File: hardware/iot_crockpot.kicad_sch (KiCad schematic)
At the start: 0 parts

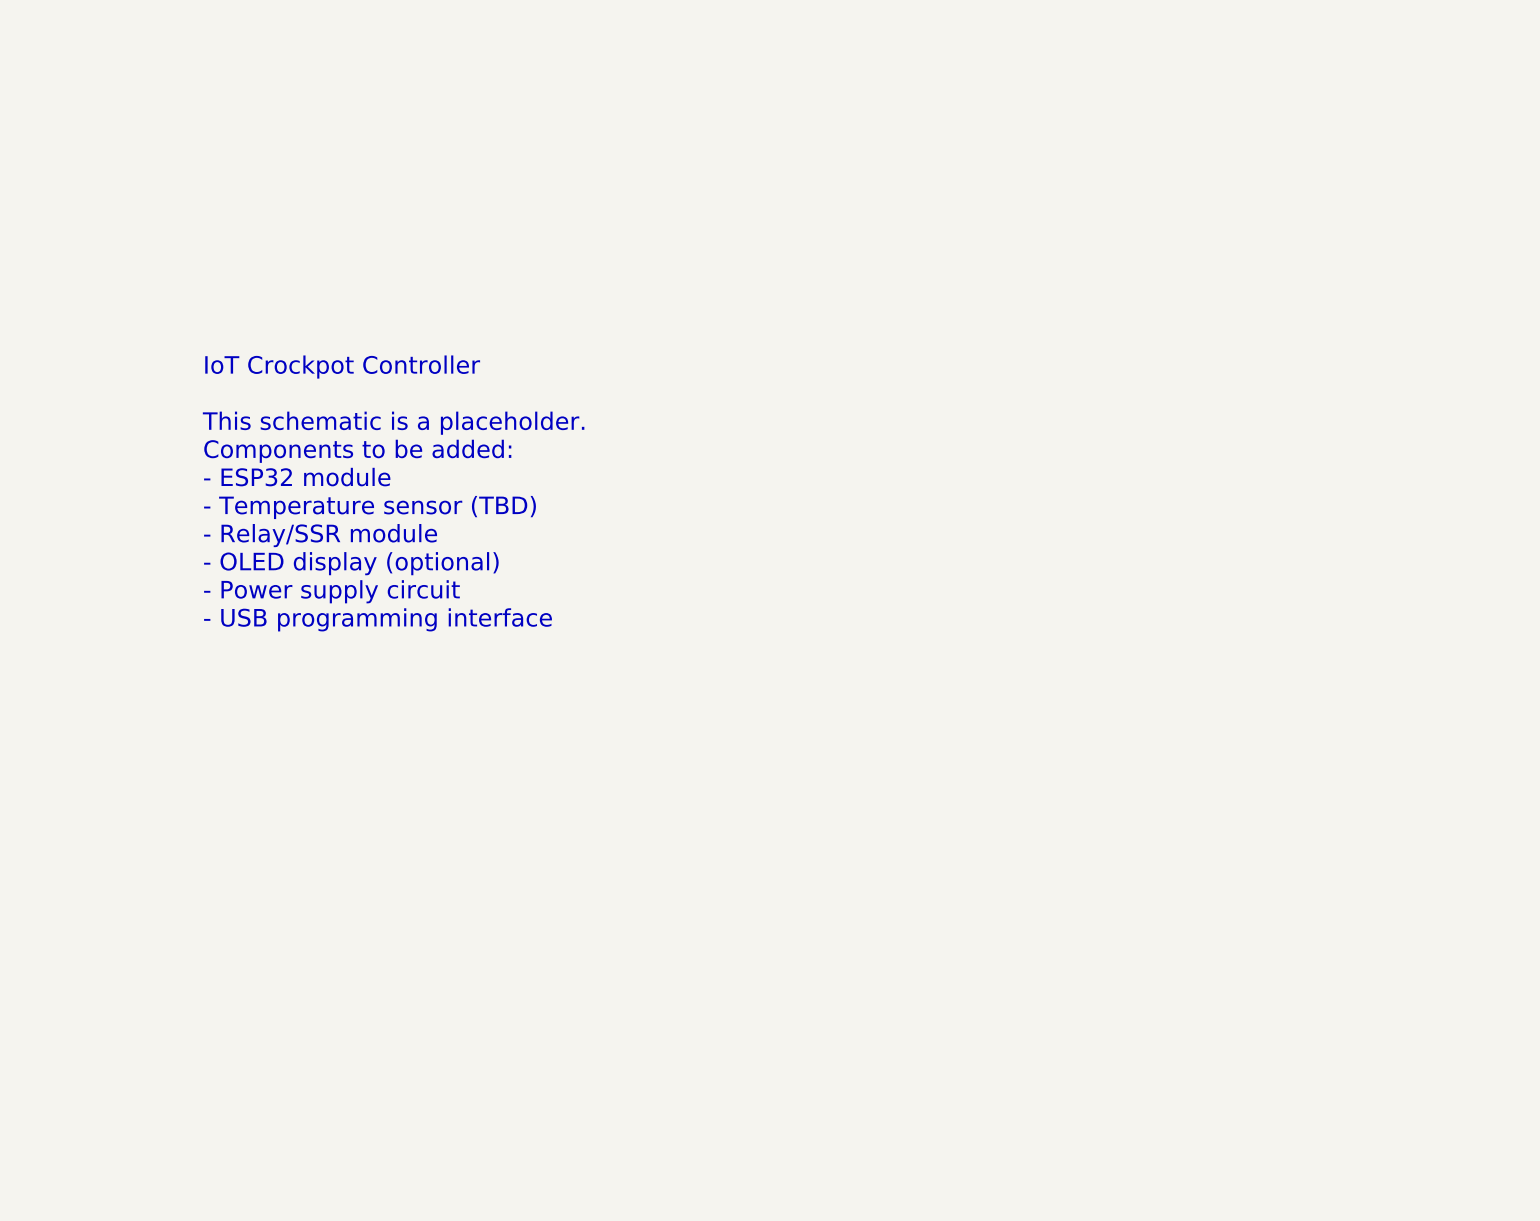
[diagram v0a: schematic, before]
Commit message: Started schematic part selection
added XIAO ESP32-C3
added HLK-PM01 120VAC to 5VDC power module
added relays
added thermal couple sensor
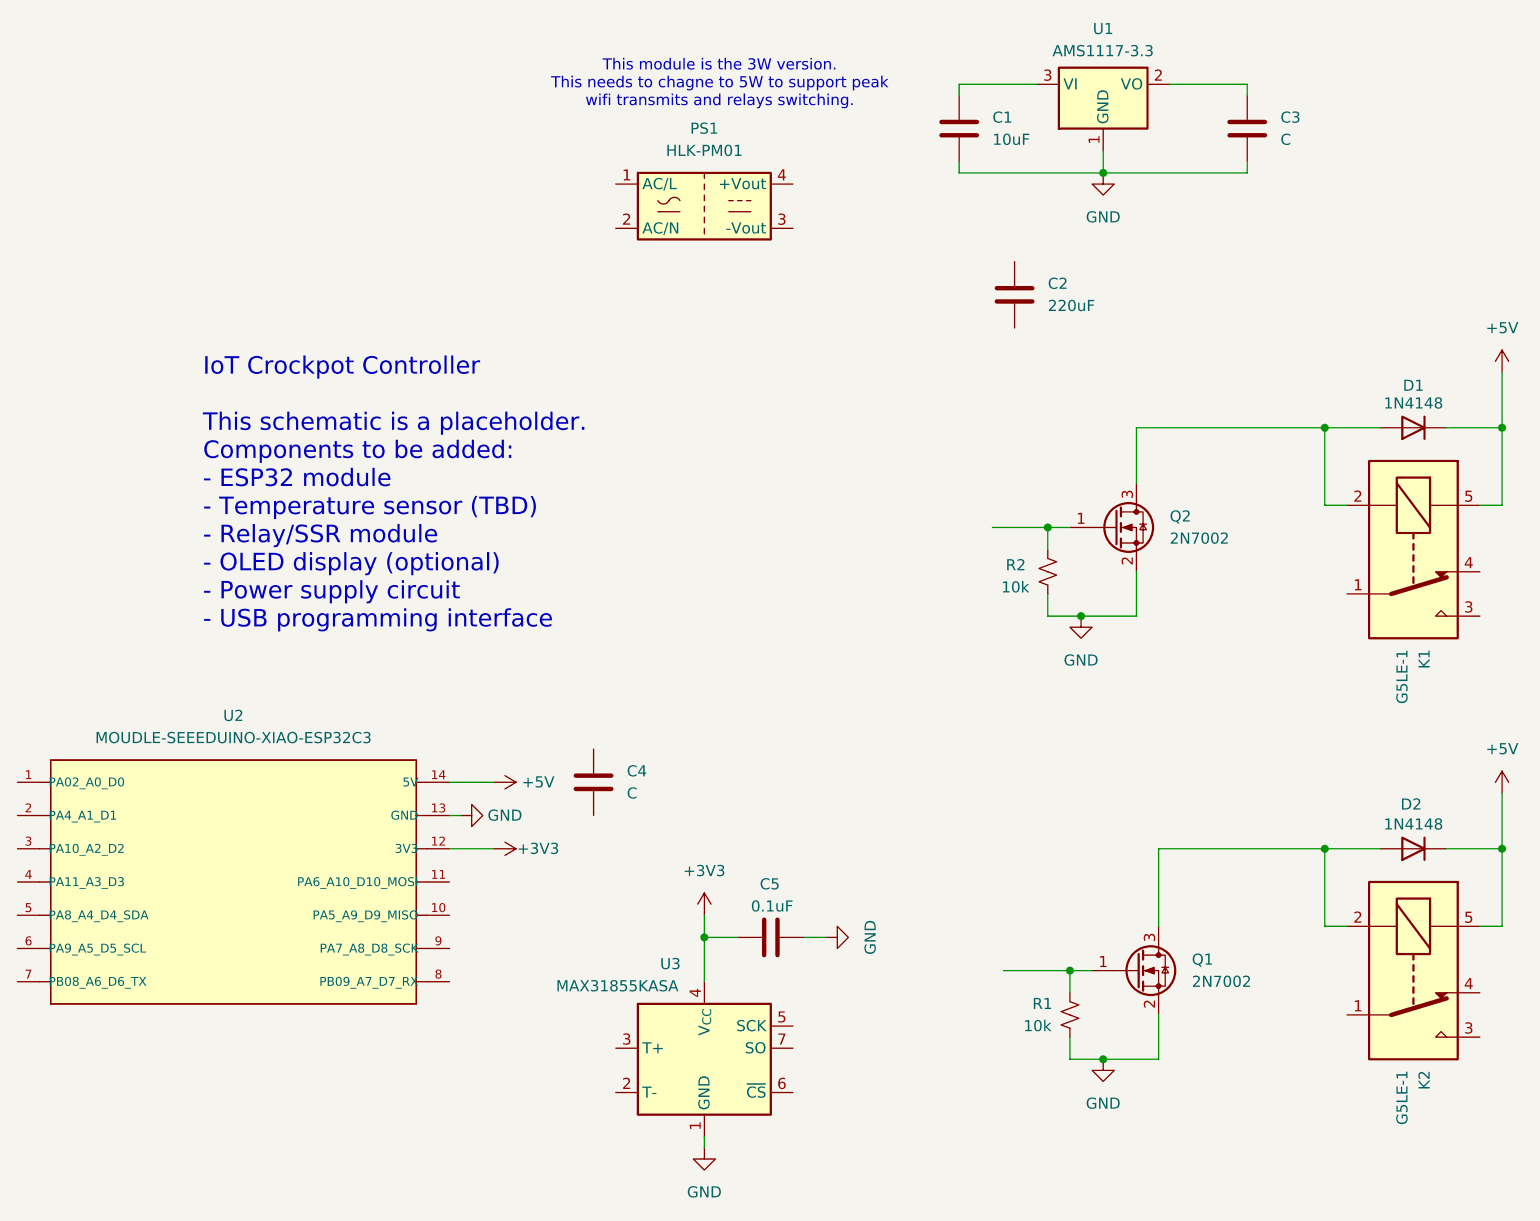
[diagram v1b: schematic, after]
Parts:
- added C1: 10uF, symbol Device:C
- added C2: 220uF, symbol Device:C
- added C3, C4: C, symbol Device:C
- added C5: 0.1uF, symbol Device:C
- added D1, D2: 1N4148, Diode_THT:D_DO-35_SOD27_P7.62mm_Horizontal, symbol Diode:1N4148
- added K1, K2: G5LE-1, Relay_THT:Relay_SPDT_Omron-G5LE-1, symbol Relay:G5LE-1
- added PS1: HLK-PM01, Converter_ACDC:Converter_ACDC_Hi-Link_HLK-PMxx, symbol Converter_ACDC:HLK-PM01
- added Q1, Q2: 2N7002, Package_TO_SOT_SMD:SOT-23, symbol Transistor_FET:2N7002
- added R1, R2: 10k, symbol Device:R_Small_US
- added U1: AMS1117-3.3, Package_TO_SOT_SMD:SOT-223-3_TabPin2, symbol Regulator_Linear:AMS1117-3.3
- added U2: MOUDLE-SEEEDUINO-XIAO-ESP32C3, XIAO-ESP32-C3:MCU_Seeed_ESP32C3_w_3D_model, symbol MOUDLE-SEEEDUINO-XIAO-ESP32C3:MOUDLE-SEEEDUINO-XIAO-ESP32C3
- added U3: MAX31855KASA, Package_SO:SOIC-8_3.9x4.9mm_P1.27mm, symbol Sensor_Temperature:MAX31855KASA
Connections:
- new net: Q2.1 (G), R2.1
- new net: D2.2 (A), K2.2, Q1.3 (D)
- new net: C3.1, U1.2 (VO)
- new net: C1.1, U1.3 (VI)
- new net: Q1.1 (G), R1.1
- new net: D1.2 (A), K1.2, Q2.3 (D)
- new net +3V3: C5.1, U2.12 (3V3), U3.4 (V_{CC})
- new net +5V: D1.1 (K), D2.1 (K), K1.5, K2.5, U2.14 (5V)
- new net GND: C1.2, C3.2, C5.2, Q1.2 (S), Q2.2 (S), R1.2, R2.2, U1.1 (GND), U2.13 (GND), U3.1 (GND)
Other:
- note added: "This module is the 3W version. This needs to chagne to 5W to support peak wifi transmits and relays switching."
